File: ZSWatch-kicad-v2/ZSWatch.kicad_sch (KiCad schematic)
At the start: 75 parts, among them IC1 ESDALC6V1W5, IC2 XC9265C181MR-G, IC3 TPS61023DRLT, IC4 MAX30101EFD+T, IC5 FAN5622SX, IC6 BMI270, IC7 LIS2MDLTR, J2 Charger and programming heade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, M1 Vibrator DC Motor, U1 MAX1811ESA+, U10 0_NORA-B106, U11 TXB0104QRUTRQ1, U12 GC9A01, U13 GC9A01A_CST816S, U2 DMC2400UV-7, U3 NCV300LSN36T1G, U4 BMP581, U5 BME688, U6 DRV2603RUNT, U7 XC9265A331MR-G

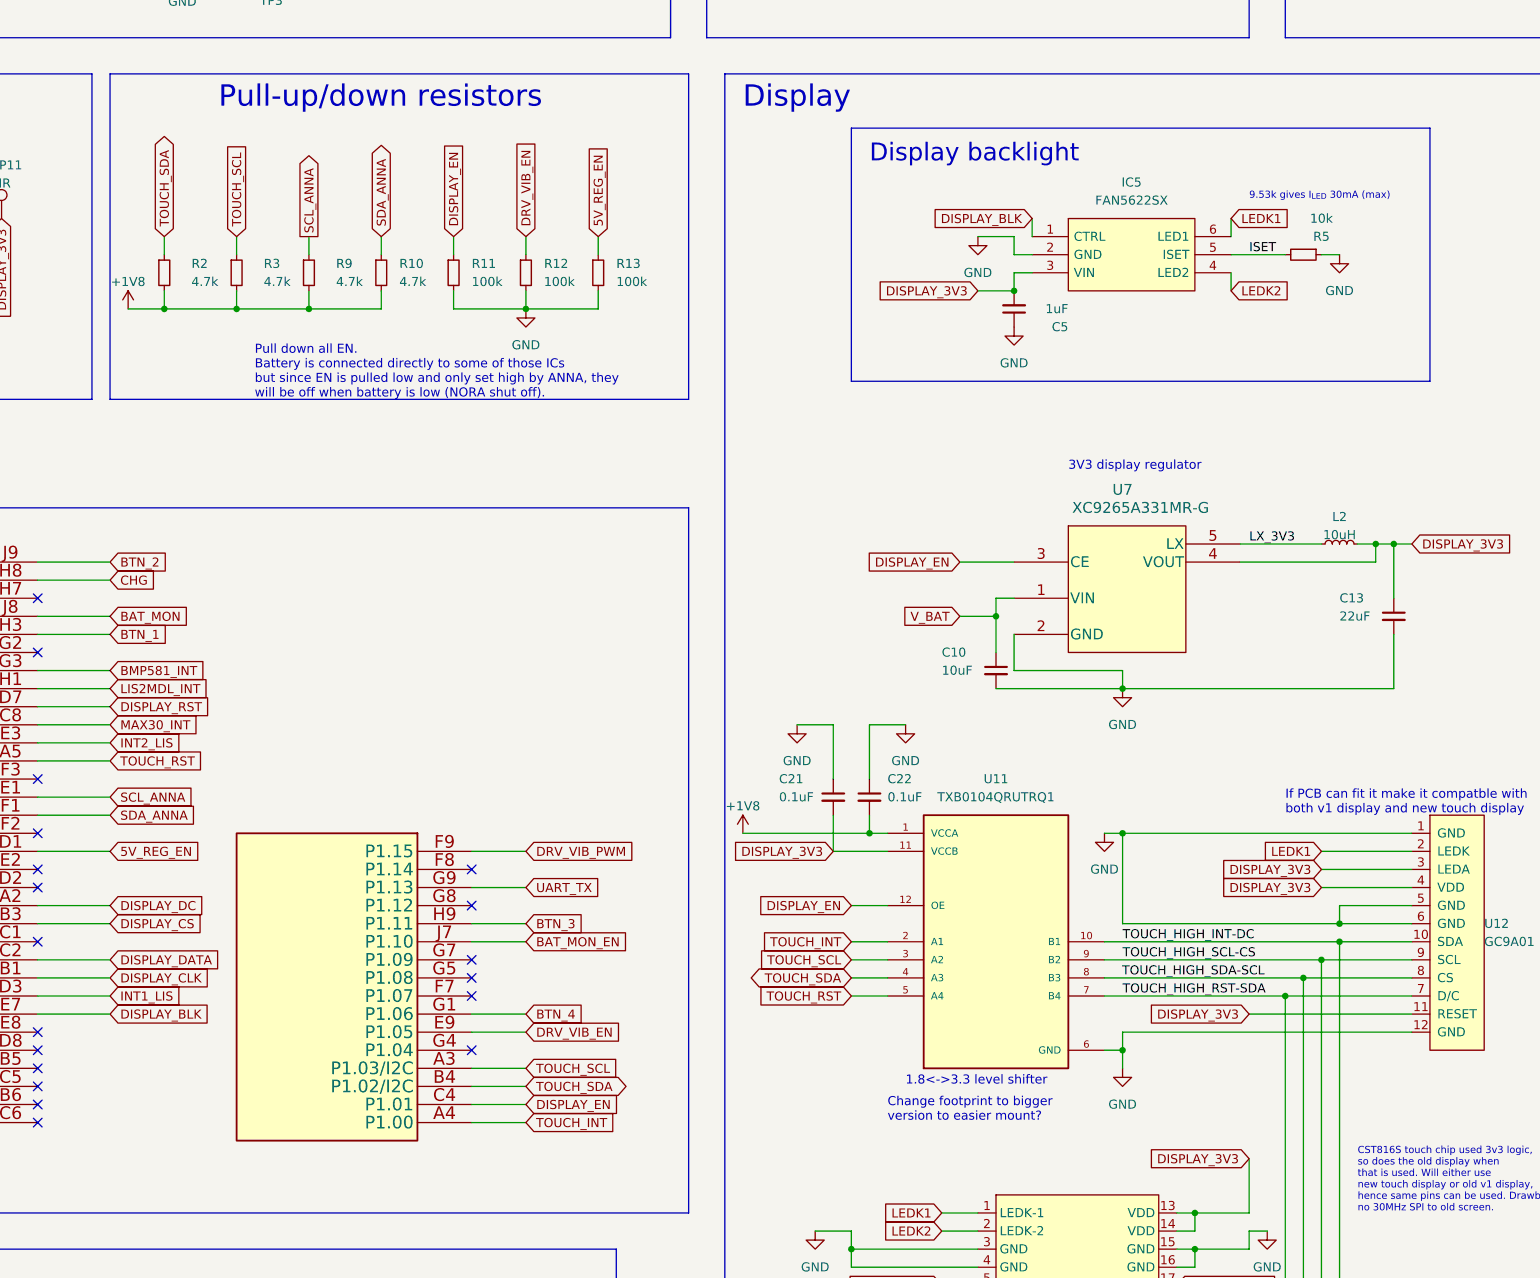
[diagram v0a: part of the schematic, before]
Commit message: Replace touch chip logic shifter with one that works with I2C.
Replace TXB0104 with pin compatible NTS0104GU12. It includes internal
pullups hence the touch I2C pin pullups are removed.

For ZSWatch without touch screen then we may still mount TXB0104 as I can see
there may be some current leakage when running SPI and using NTS0104 due to it's
internal pullups. Will test this later.
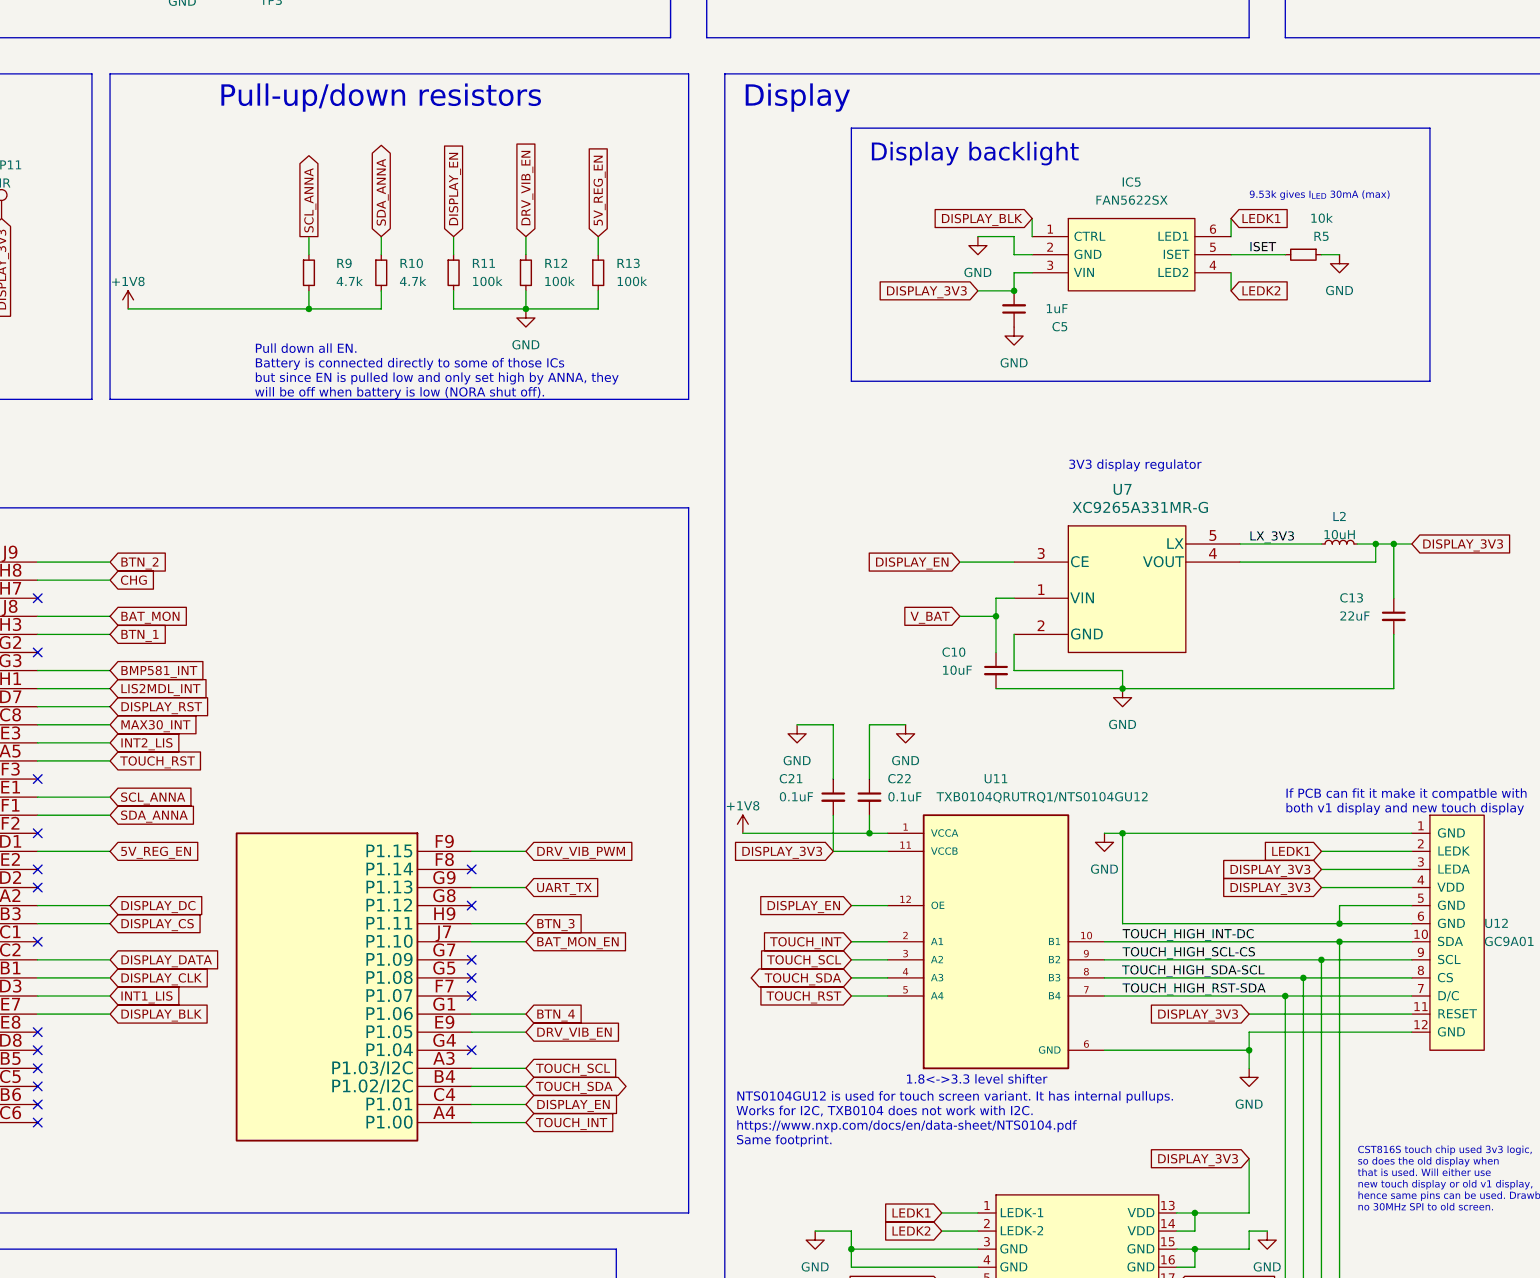
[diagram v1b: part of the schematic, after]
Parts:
- removed R2, R3: 4.7k, Resistor_SMD:R_0603_1608Metric, symbol Device:R_Small
- U11: value TXB0104QRUTRQ1 -> TXB0104QRUTRQ1/NTS0104GU12; Alt buy (none) -> https://www.digikey.se/en/products/detail/nxp-usa-inc/NTS01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; Alt datasheet (none) -> https://www.nxp.com/docs/en/data-sheet/NTS0104.pdf; Version for touch variant (none) -> NTS0104GU12
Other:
- note added: "NTS0104GU12 is used for touch screen variant. It has internal pullups. Works for I2C, TXB0104 does not work with I2C. https://www.nxp.com/docs/en/data-sheet/NTS0104.pdf Same footprint."
- note removed: "Change footprint to bigger version to easier mount?"
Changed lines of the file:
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@@
   (junction (at 314.96 254) (diameter 0) (color 0 0 0 0)
   )
-  (junction (at 157.48 157.48) (diameter 0) (color 0 0 0 0)
-  )
   (junction (at 317.5 251.46) (diameter 0) (color 0 0 0 0)
   )
@@
   (junction (at 302.26 284.48) (diameter 0) (color 0 0 0 0)
   )
-  (junction (at 167.64 157.48) (diameter 0) (color 0 0 0 0)
-  )
   (junction (at 457.2 203.2) (diameter 0) (color 0 0 0 0)
   )
@@
   (junction (at 322.58 246.38) (diameter 0) (color 0 0 0 0)
   )
-  (junction (at 292.1 261.62) (diameter 0) (color 0 0 0 0)
-  )
   (junction (at 467.36 241.3) (diameter 0) (color 0 0 0 0)
   )
@@
   (junction (at 330.2 190.5) (diameter 0) (color 0 0 0 0)
   )
+  (junction (at 309.88 261.62) (diameter 0) (color 0 0 0 0)
+  )
   (junction (at 88.9 233.68) (diameter 0) (color 0 0 0 0)
   )
@@
     (stroke (width 0) (type default) (color 0 0 0 0))
   )
-  (wire (pts (xy 289.56 261.62) (xy 292.1 261.62))
-    (stroke (width 0) (type default) (color 0 0 0 0))
-  )
   (wire (pts (xy 276.86 91.44) (xy 279.4 91.44))
     (stroke (width 0) (type default) (color 0 0 0 0))
@@
     (stroke (width 0) (type default) (color 0 0 0 0))
   )
-  (wire (pts (xy 157.48 157.48) (xy 152.4 157.48))
-    (stroke (width 0) (type default) (color 0 0 0 0))
-  )
   (polyline (pts (xy 231.14 284.48) (xy 15.24 284.48))
     (stroke (width 0) (type default) (color 0 0 0 0))
@@
     (stroke (width 0) (type default) (color 0 0 0 0))
   )
-  (wire (pts (xy 167.64 157.48) (xy 177.8 157.48))
+  (wire (pts (xy 152.4 157.48) (xy 177.8 157.48))
     (stroke (width 0) (type default) (color 0 0 0 0))
   )
@@
     (stroke (width 0) (type default) (color 0 0 0 0))
   )
+  (wire (pts (xy 289.56 261.62) (xy 309.88 261.62))
+    (stroke (width 0) (type default) (color 0 0 0 0))
+  )
   (polyline (pts (xy 228.6 119.38) (xy 15.24 119.38))
     (stroke (width 0) (type default) (color 0 0 0 0))
@@
     (stroke (width 0) (type default) (color 0 0 0 0))
   )
-  (wire (pts (xy 292.1 259.08) (xy 292.1 261.62))
+  (wire (pts (xy 309.88 259.08) (xy 309.88 261.62))
     (stroke (width 0) (type default) (color 0 0 0 0))
   )
@@
     (stroke (width 0) (type default) (color 0 0 0 0))
   )
-  (wire (pts (xy 292.1 261.62) (xy 292.1 264.16))
+  (wire (pts (xy 309.88 261.62) (xy 309.88 264.16))
     (stroke (width 0) (type default) (color 0 0 0 0))
   )
@@
     (stroke (width 0) (type default) (color 0 0 0 0))
   )
-  (wire (pts (xy 157.48 157.48) (xy 167.64 157.48))
-    (stroke (width 0) (type default) (color 0 0 0 0))
-  )
   (wire (pts (xy 160.02 93.98) (xy 154.94 93.98))
     (stroke (width 0) (type default) (color 0 0 0 0))
@@
     (stroke (width 0) (type default) (color 0 0 0 0))
   )
-  (wire (pts (xy 167.64 147.32) (xy 167.64 149.86))
-    (stroke (width 0) (type default) (color 0 0 0 0))
-  )
   (wire (pts (xy 459.74 93.98) (xy 452.12 93.98))
     (stroke (width 0) (type default) (color 0 0 0 0))
@@
     (stroke (width 0) (type default) (color 0 0 0 0))
   )
-  (wire (pts (xy 167.64 154.94) (xy 167.64 157.48))
-    (stroke (width 0) (type default) (color 0 0 0 0))
-  )
   (wire (pts (xy 149.86 307.34) (xy 147.32 307.34))
     (stroke (width 0) (type default) (color 0 0 0 0))
@@
     (stroke (width 0) (type default) (color 0 0 0 0))
   )
-  (wire (pts (xy 157.48 154.94) (xy 157.48 157.48))
-    (stroke (width 0) (type default) (color 0 0 0 0))
-  )
   (polyline (pts (xy 485.14 264.16) (xy 363.22 264.16))
     (stroke (width 0) (type default) (color 0 0 0 0))
@@
     (stroke (width 0) (type default) (color 0 0 0 0))
   )
-  (wire (pts (xy 157.48 147.32) (xy 157.48 149.86))
-    (stroke (width 0) (type default) (color 0 0 0 0))
-  )
   (wire (pts (xy 302.26 284.48) (xy 299.72 284.48))
     (stroke (width 0) (type default) (color 0 0 0 0))
@@
     (stroke (width 0) (type default) (color 0 0 0 0))
   )
-  (wire (pts (xy 332.74 259.08) (xy 292.1 259.08))
+  (wire (pts (xy 332.74 259.08) (xy 309.88 259.08))
     (stroke (width 0) (type default) (color 0 0 0 0))
   )
@@
     (effects (font (size 1.27 1.27)) (justify left bottom))
   )
-  (text "Change footprint to bigger\nversion to easier mount?"
-    (at 259.08 271.78 0)
+  (text "NTS0104GU12 is used for touch screen variant. It has internal pullups.\nWorks for I2C, TXB0104 does not work with I2C.\nhttps://www.nxp.com/docs/en/data-sheet/NTS0104.pdf\nSame footprint."
+    (at 237.8198 275.2248 0)
     (effects (font (size 1.27 1.27)) (justify left bottom))
   )
@@
     )
   )
-  (global_label "TOUCH_SDA" (shape bidirectional) (at 157.48 147.32 90) (fields_autoplaced)
-    (effects (font (size 1.27 1.27)) (justify left))
-    (property "Intersheet References" "${INTERSHEET_REFS}" (id 0) (at 157.5594 134.1421 90)
-      (effects (font (size 1.27 1.27)) (justify left) hide)
-    )
-  )
   (global_label "RESET_N" (shape input) (at 30.48 251.46 180) (fields_autoplaced)
     (effects (font (size 1.27 1.27)) (justify right))
@@
     )
   )
-  (global_label "TOUCH_SCL" (shape input) (at 167.64 147.32 90) (fields_autoplaced)
-    (effects (font (size 1.27 1.27)) (justify left))
-    (property "Intersheet References" "${INTERSHEET_REFS}" (id 0) (at 167.7194 134.2026 90)
-      (effects (font (size 1.27 1.27)) (justify left) hide)
-    )
-  )
   (global_label "CHG" (shape input) (at 149.86 195.58 0) (fields_autoplaced)
     (effects (font (size 1.27 1.27)) (justify left))
@@
   )
   (symbol (lib_id "user_library:TXB0104QRUTRQ1") (at 274.32 246.38 0) (unit 1)
-    (in_bom yes) (on_board yes) (fields_autoplaced)
+    (in_bom yes) (on_board yes)
     (property "Reference" "U11" (id 0) (at 274.32 223.52 0))
-    (property "Value" "TXB0104QRUTRQ1" (id 1) (at 274.32 226.06 0))
+    (property "Value" "TXB0104QRUTRQ1/NTS0104GU12" (id 1) (at 280.8735 226.0542 0))
     (property "Footprint" "SamacSys_Parts:HPA01164RUTR" (id 2) (at 274.32 246.38 0)
       (effects (font (size 1.27 1.27)) (justify left bottom) hide)
@@
       (effects (font (size 1.27 1.27)) hide)
     )
+    (property "Version for touch variant" "NTS0104GU12" (id 11) (at 274.32 246.38 0)
+      (effects (font (size 1.27 1.27)) hide)
+    )
+    (property "Alt datasheet" "https://www.nxp.com/docs/en/data-sheet/NTS0104.pdf" (id 12) (at 274.32 246.38 0)
+      (effects (font (size 1.27 1.27)) hide)
+    )
+    (property "Alt buy" "https://www.digikey.se/en/products/detail/nxp-usa-inc/NTS0104GU12-115/2763907" (id 13) (at 274.32 246.38 0)
+      (effects (font (size 1.27 1.27)) hide)
+    )
     (pin "1")
     (pin "10")
@@
     (pin "1")
   )
-  (symbol (lib_id "power:GND") (at 292.1 264.16 0) (unit 1)
+  (symbol (lib_id "power:GND") (at 309.88 264.16 0) (unit 1)
     (in_bom yes) (on_board yes)
-    (property "Reference" "#PWR0113" (id 0) (at 292.1 270.51 0)
+    (property "Reference" "#PWR0113" (id 0) (at 309.88 270.51 0)
       (effects (font (size 1.27 1.27)) hide)
     )
-    (property "Value" "GND" (id 1) (at 292.1 269.24 0))
-    (property "Footprint" "" (id 2) (at 292.1 264.16 0)
+    (property "Value" "GND" (id 1) (at 309.88 269.24 0))
+    (property "Footprint" "" (id 2) (at 309.88 264.16 0)
       (effects (font (size 1.27 1.27)) hide)
     )
-    (property "Datasheet" "" (id 3) (at 292.1 264.16 0)
+    (property "Datasheet" "" (id 3) (at 309.88 264.16 0)
       (effects (font (size 1.27 1.27)) hide)
     )
@@
     (pin "1")
   )
-  (symbol (lib_id "Device:R_Small") (at 167.64 152.4 0) (unit 1)
-    (in_bom yes) (on_board yes)
-    (property "Reference" "R3" (id 0) (at 171.45 151.1299 0)
-      (effects (font (size 1.27 1.27)) (justify left))
-    )
-    (property "Value" "4.7k" (id 1) (at 171.45 153.6699 0)
-      (effects (font (size 1.27 1.27)) (justify left))
-    )
-    (property "Footprint" "Resistor_SMD:R_0603_1608Metric" (id 2) (at 167.64 152.4 0)
-      (effects (font (size 1.27 1.27)) hide)
-    )
-    (property "Datasheet" "~" (id 3) (at 167.64 152.4 0)
-      (effects (font (size 1.27 1.27)) hide)
-    )
-    (pin "1")
-    (pin "2")
-  )
   (symbol (lib_id "power:GND") (at 88.9 276.86 0) (unit 1)
     (in_bom yes) (on_board yes)
@@
     (pin "1")
   )
-  (symbol (lib_id "Device:R_Small") (at 157.48 152.4 0) (unit 1)
-    (in_bom yes) (on_board yes)
-    (property "Reference" "R2" (id 0) (at 161.29 151.1299 0)
-      (effects (font (size 1.27 1.27)) (justify left))
-    )
-    (property "Value" "4.7k" (id 1) (at 161.29 153.6699 0)
-      (effects (font (size 1.27 1.27)) (justify left))
-    )
-    (property "Footprint" "Resistor_SMD:R_0603_1608Metric" (id 2) (at 157.48 152.4 0)
-      (effects (font (size 1.27 1.27)) hide)
-    )
-    (property "Datasheet" "~" (id 3) (at 157.48 152.4 0)
-      (effects (font (size 1.27 1.27)) hide)
-    )
-    (pin "1")
-    (pin "2")
-  )
   (symbol (lib_id "power:GND") (at 43.18 40.64 0) (unit 1)
     (in_bom yes) (on_board yes)
@@
       (reference "R1") (unit 1) (value "10k") (footprint "Resistor_SMD:R_0603_1608Metric")
     )
-    (path "/be73a52b-9cfb-4ee5-9baa-a0e60d252b2c"
-      (reference "R2") (unit 1) (value "4.7k") (footprint "Resistor_SMD:R_0603_1608Metric")
-    )
-    (path "/54d20038-2c09-483c-9b19-7046d6466ace"
-      (reference "R3") (unit 1) (value "4.7k") (footprint "Resistor_SMD:R_0603_1608Metric")
-    )
     (path "/8e1d8114-c46a-45cc-88e3-7abfbdcfb36e"
       (reference "R4") (unit 1) (value "1M0") (footprint "Resistor_SMD:R_0603_1608Metric")
@@
     )
     (path "/19dfefc0-dc07-4bb3-8b08-909b7b408eba"
-      (reference "U11") (unit 1) (value "TXB0104QRUTRQ1") (footprint "SamacSys_Parts:HPA01164RUTR")
+      (reference "U11") (unit 1) (value "TXB0104QRUTRQ1/NTS0104GU12") (footprint "SamacSys_Parts:HPA01164RUTR")
     )
     (path "/17718185-4713-460e-81c8-951c063ac884"

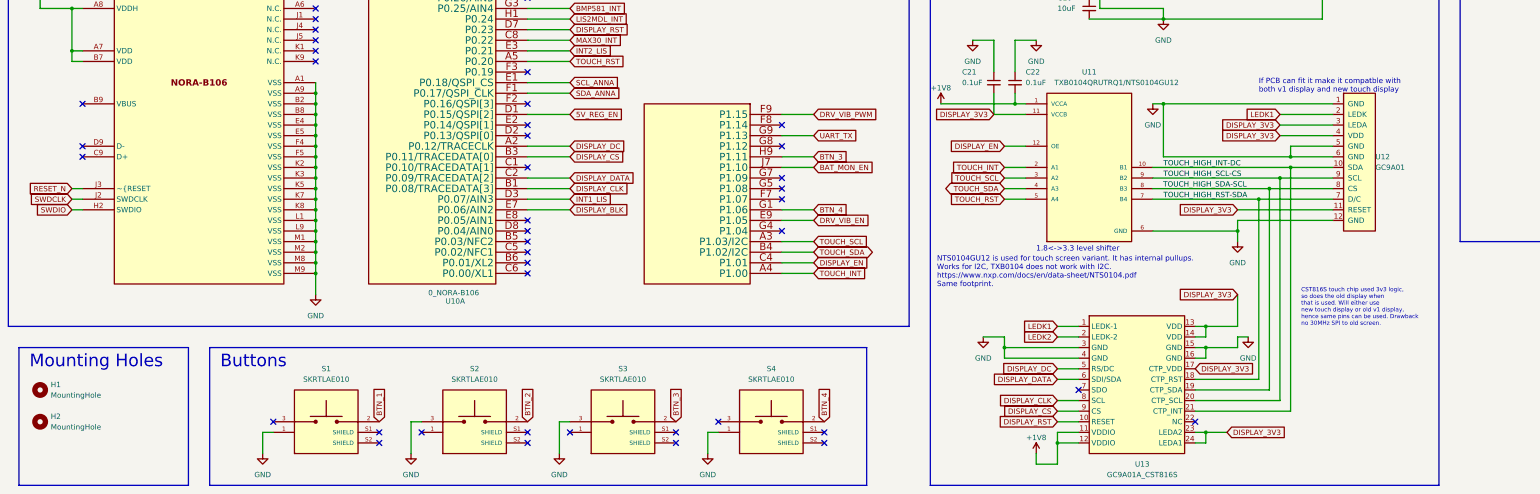
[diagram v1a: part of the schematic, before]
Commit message: Move display connector so there is no strain on the cable. From now on only touch screen is supported. Remove none touch screen connector as it does not fit anymore.
The moving of touch display connector caused a bit of re-routing. Without redoing alot of the routing
we need the space used by the connector to the none touch screen. From now on only touch screen is supported.
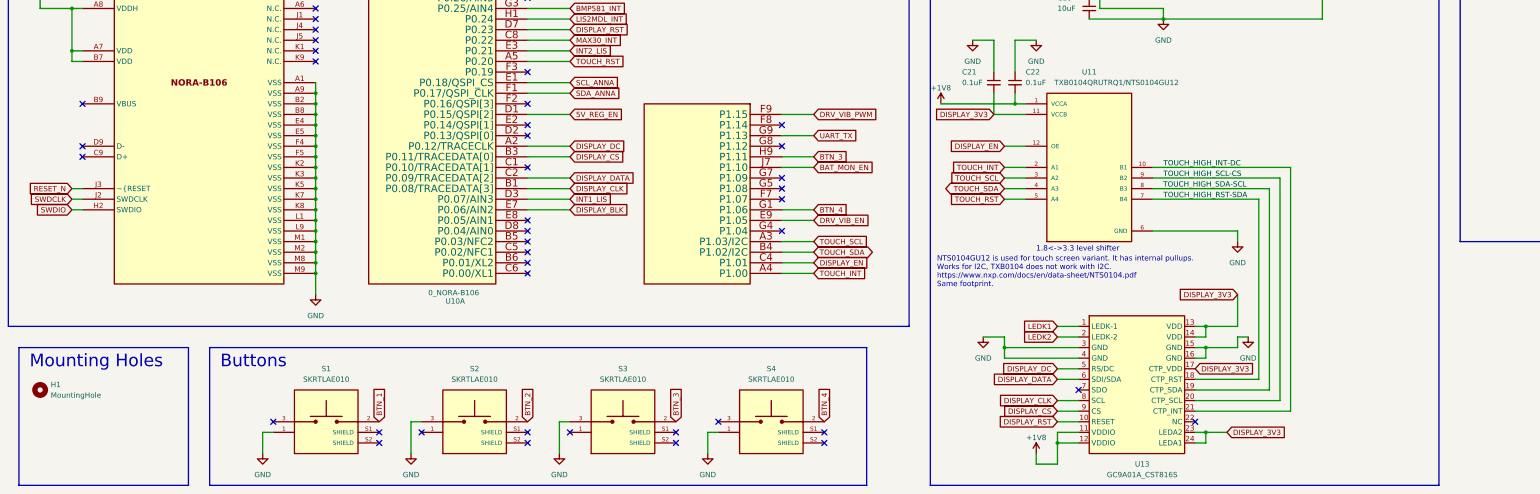
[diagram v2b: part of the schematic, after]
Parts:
- removed H2: MountingHole, MountingHole:MountingHole_2.2mm_M2, symbol Mechanical:MountingHole
- removed U12: GC9A01, user_library:GC9A01_disp_smaller, symbol user_library:GC9A01
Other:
- note removed: "CST816S touch chip used 3v3 logic, so does the old display when that is used. Will either use new touch display or old v1 display, hence same pins can be used. Drawback no 30MHz SPI to old screen."
- note removed: "If PCB can fit it make it compatble with both v1 display and new touch display"
